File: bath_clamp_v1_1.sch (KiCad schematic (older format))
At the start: 66 parts, among them J1 105-1103-001, J2 105-1103-001, J3 105-1103-001, K1 1462042-8, K2 1462042-8, Q1 MBT3904DW1T1G, Q3 MBT3904DW1T1G, Q4 MBT3904DW1T1G, U1 OPA828, U12 TCA9555DBR, U13 TCA9555DBR, U2 ADG1208, U3 G6L-1F-TR-DC5, U4 G6L-1F-TR-DC5, U5 G6L-1F-TR-DC5

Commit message: made sheet for Howland
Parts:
- removed C?: 5p, Capacitor_SMD:C_0603_1608Metric, symbol Device:C
- removed C? (x2): 0.1u, Capacitor_SMD:C_0603_1608Metric, symbol Device:C
- removed R? (x4): 1M, Resistor_SMD:R_0603_1608Metric, symbol Device:R_US
- removed U?: OPA991S, Package_TO_SOT_SMD:SOT-23-6, symbol covg-kicad:OPA991S
- J4: renamed from J?; footprint (none) -> bath_clamp_v1:HDMI_A
- U19: renamed from U?; footprint PW16_TEX -> Package_SO:TSSOP-16_4.4x5mm_P0.65mm
- gave numbers to parts that had none: 9
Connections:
- wire segments 347 -> 321
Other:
- note removed: "50 nA to 10 uA\n=> 50 mV to 10 V"
- note removed: "Howland Current Pump\nTexas Instrument AN-1515\nR matching sets output impedance\nUse 0.1% tol. Rs"
- note removed: "SDOWN referenced to V-\ninternal pull-down\n"
- moved on the sheet: C29, C30

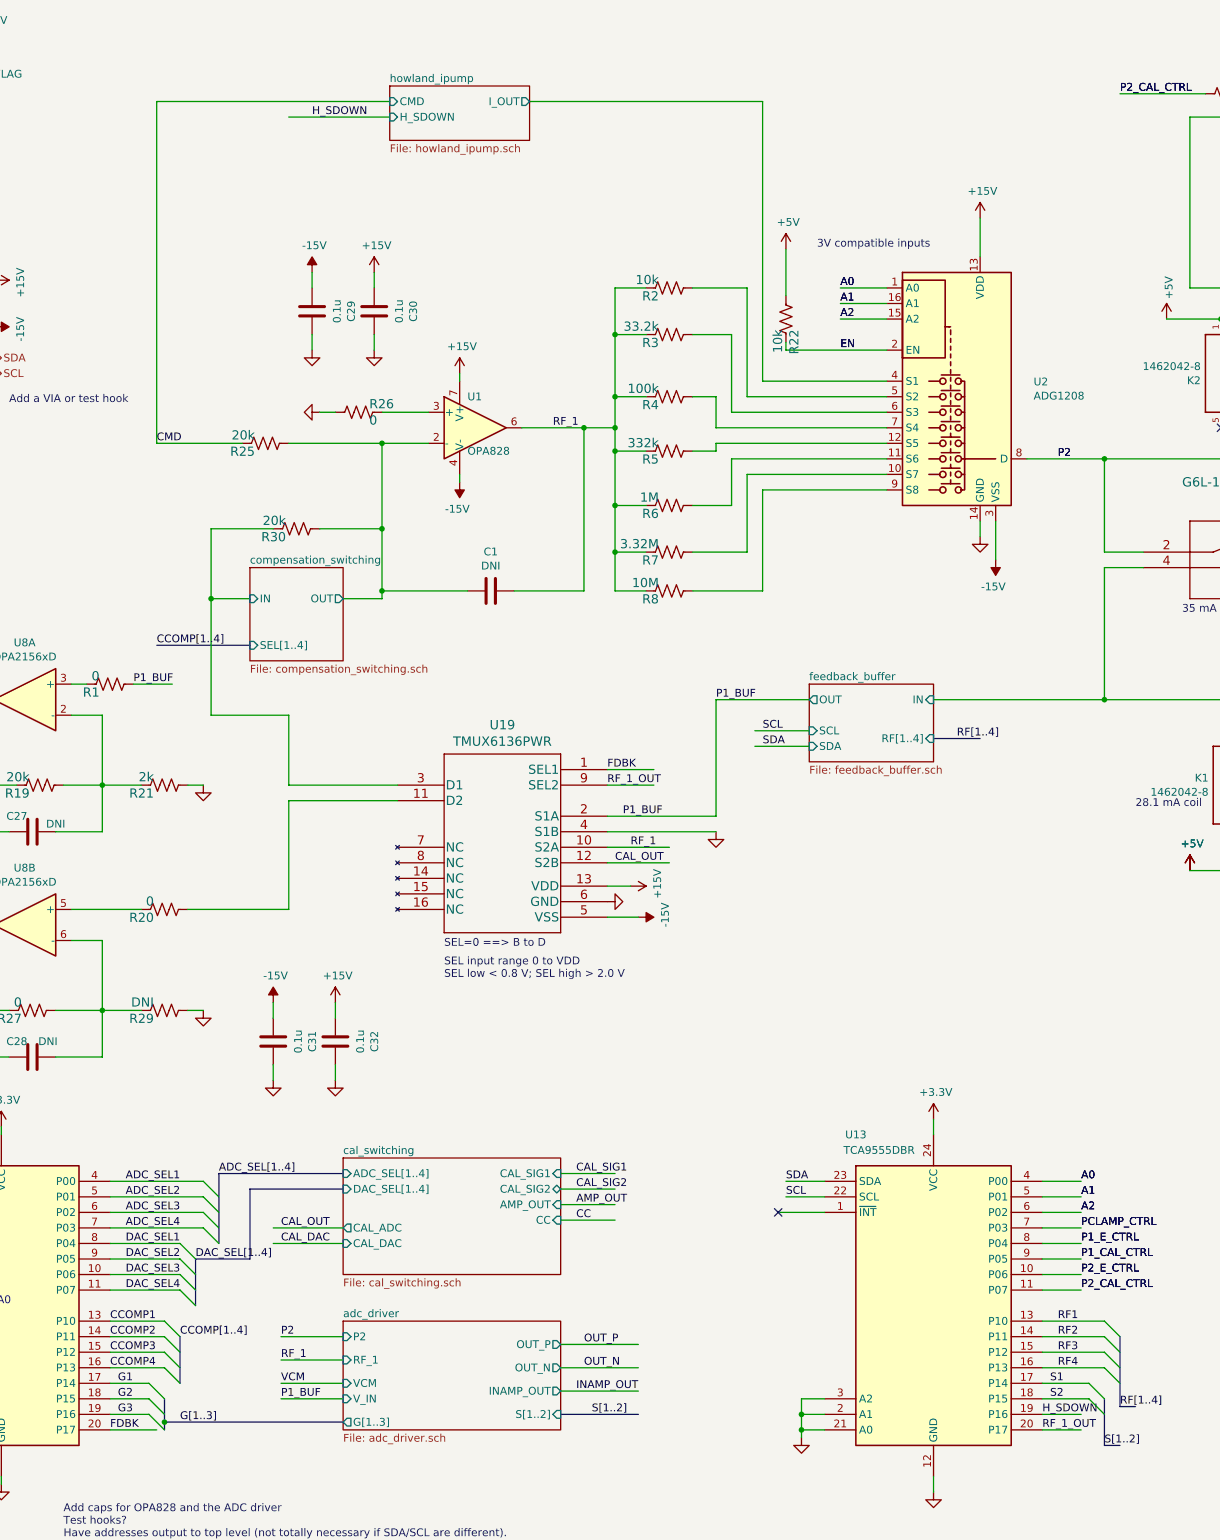
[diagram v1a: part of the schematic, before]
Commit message: removed all references to clamp footprints
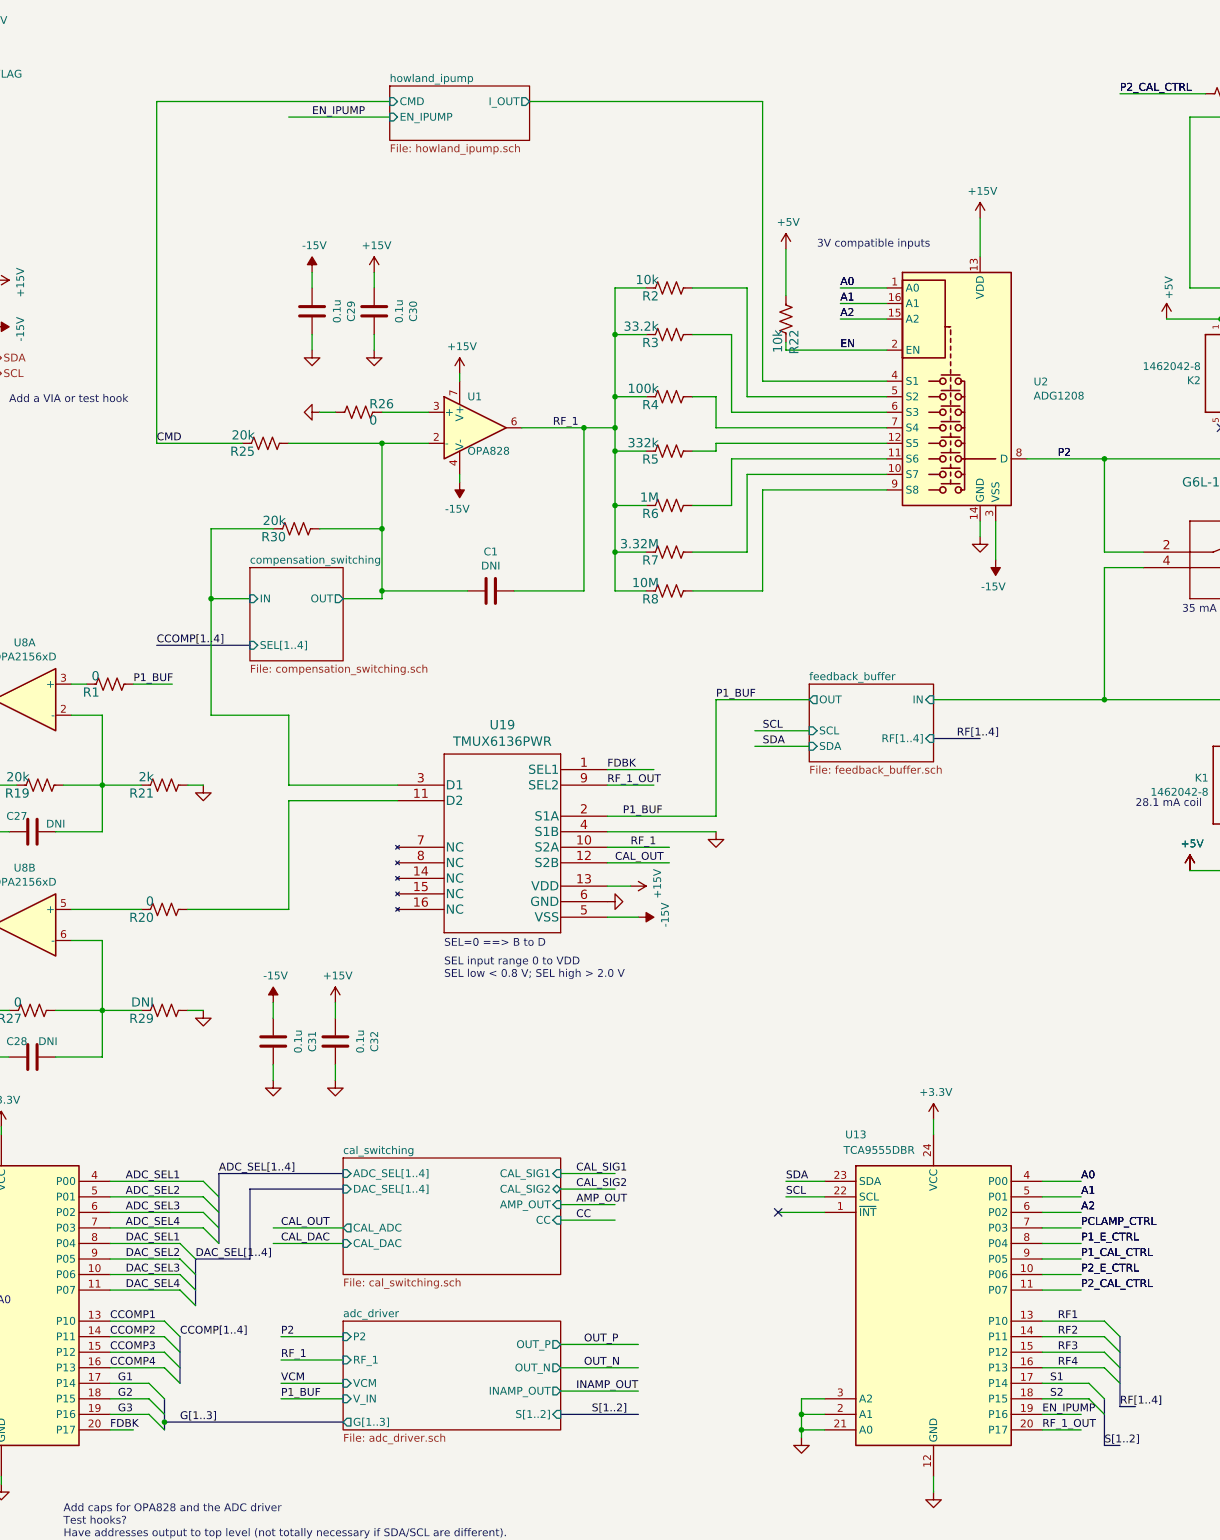
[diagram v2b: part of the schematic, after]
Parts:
- J4: footprint bath_clamp_v1:HDMI_A -> covg-kicad:HDMI_A
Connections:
- net labels added: EN_IPUMP
- net labels removed: H_SDOWN
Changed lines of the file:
@@
 	8800 9550 9050 9550
 Text Label 8800 9550 0    50   ~ 0
-H_SDOWN
+EN_IPUMP
 Wire Wire Line
 	6000 5400 6300 5400
@@
 	3150 9600 3150 9650
 Wire Wire Line
-	2800 9650 3100 9650
-Wire Wire Line
 	6000 5800 6700 5800
 $Comp
@@
 F 0 "J4" H 1680 2496 50  0000 L CNN
 F 1 "HDMI_A" H 1680 2405 50  0000 L CNN
-F 2 "bath_clamp_v1:HDMI_A" H 1275 2450 50  0001 C CNN
+F 2 "covg-kicad:HDMI_A" H 1275 2450 50  0001 C CNN
 F 3 "https://en.wikipedia.org/wiki/HDMI" H 1275 2450 50  0001 C CNN
 	1    1250 2450
@@
 F2 "I_OUT" O R 5500 1100 50
 F3 "CMD" I L 4600 1100 50
-F4 "H_SDOWN" I L 4600 1200 50
+F4 "EN_IPUMP" I L 4600 1200 50
 $EndSheet
 Wire Wire Line
@@
 Wire Wire Line
 	4600 1200 3950 1200
+Text Label 4100 1200 0    50   ~ 0
+EN_IPUMP
+Wire Wire Line
+	2800 9650 2950 9650
 Wire Bus Line
 	9200 9450 9200 9750
@@
 Wire Bus Line
 	3500 8000 3500 8450
-Text Label 4100 1200 0    50   ~ 0
-H_SDOWN
 $EndSCHEMATC

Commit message: layout updates; part positioning
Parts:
- added C36, C38: 0.1u, Capacitor_SMD:C_0603_1608Metric, symbol Device:C
- added C37: DNI, Capacitor_SMD:C_0603_1608Metric, symbol Device:C
- added R63: 30k, Resistor_SMD:R_0603_1608Metric, symbol Device:R_US
- added R64: 3k, Resistor_SMD:R_0603_1608Metric, symbol Device:R_US
- added R67, R69, R70: DNI, Resistor_SMD:R_0603_1608Metric, symbol Device:R_US
- added U25: OPA2156xD, Package_SO:SOIC-8_3.9x4.9mm_P1.27mm, symbol Amplifier_Operational:OPA2156xD
- J4: footprint covg-kicad:HDMI_A -> covg-kicad:CONN_10029449-111RLF_HDMI_A
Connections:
- net labels added: CMD_BUF
- wire segments 321 -> 353
- no-connect marks 5 -> 6
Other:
- note added: "Gain by x10 on cable\nAnd down by x10 on brd\nto reduce cable cross-talk"
- moved on the sheet: C1, C29, C30, J4, R25, R26

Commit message: layout updates and 3d models
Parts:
- added TP? (x8): RCT-0C, digikey-footprints:PROBE_PAD_0805, symbol dk_Test-Points:RCT-0C
- Q1, Q3, Q4: footprint digikey-footprints:SOT-363 -> Package_TO_SOT_SMD:SOT-363_SC-70-6
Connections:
- net labels added: F_MUX_OUT, P1, P1_OUT, P2_OUT, V_GND
- wire segments 353 -> 360
- no-connect marks 6 -> 5
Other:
- note added: "Gain by x10 on cable\nAnd down by x10 on brd\nto reduce impact of \ncable cross-talk"
- note removed: "Add a VIA or test hook"
- note removed: "Gain by x10 on cable\nAnd down by x10 on brd\nto reduce cable cross-talk"

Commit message: updates to README
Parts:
- added C39, C40: 0.1u, Capacitor_SMD:C_0603_1608Metric, symbol Device:C
- J4: Manf# (none) -> 10029449-111RLF
- TP1, TP2, TP3, TP4, TP5, TP6, TP7, TP8: renamed from TP?; Manf# (none) -> RCT-0C
- U12, U13: Manf# (none) -> TCA9555DBR
- U19: Manf# (none) -> TMUX6136PWR
- U25, U8: Manf# (none) -> OPA2156IDR
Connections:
- net labels added: A0_EXP0, A0_EXP1, A1_EXP0, A1_EXP1, A2_EXP0, A2_EXP1
- wire segments 360 -> 358
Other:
- note added: "110"
- note added: "Addr = \n0100_A2_A1_A0"
- note removed: "Add caps for OPA828 and the ADC driver\nTest hooks?\nHave addresses output to top level (not totally necessary if SDA/SCL are different). \n Buffer out calibration switching block."
- note removed: "Addr = 0100_A2_A1_A0"
- moved on the sheet: C31

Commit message: freerouter updates; close to submission
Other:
- moved on the sheet: C30, C37, R69
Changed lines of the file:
@@
 L power:+15V #PWR0154
 U 1 1 61EC7018
-P 5250 1950
+P 5300 1950
 AR Path="/6032F251/61EC7018" Ref="#PWR0154"  Part="1"
 AR Path="/6032F251/608FDC40/61EC7018" Ref="#PWR?"  Part="1"
-F 0 "#PWR0154" H 5250 1800 50  0001 C CNN
-F 1 "+15V" H 5265 2123 50  0000 C CNN
-F 2 "" H 5250 1950 50  0001 C CNN
-F 3 "" H 5250 1950 50  0001 C CNN
-	1    5250 1950
+F 0 "#PWR0154" H 5300 1800 50  0001 C CNN
+F 1 "+15V" H 5315 2123 50  0000 C CNN
+F 2 "" H 5300 1950 50  0001 C CNN
+F 3 "" H 5300 1950 50  0001 C CNN
+	1    5300 1950
 	1    0    0    -1
 $EndComp
@@
 L power:GND #PWR0155
 U 1 1 61EC701E
-P 5250 2450
+P 5300 2450
 AR Path="/6032F251/61EC701E" Ref="#PWR0155"  Part="1"
 AR Path="/6032F251/608FDC40/61EC701E" Ref="#PWR?"  Part="1"
-F 0 "#PWR0155" H 5250 2200 50  0001 C CNN
-F 1 "GND" V 5255 2322 50  0001 R CNN
-F 2 "" H 5250 2450 50  0001 C CNN
-F 3 "" H 5250 2450 50  0001 C CNN
-	1    5250 2450
+F 0 "#PWR0155" H 5300 2200 50  0001 C CNN
+F 1 "GND" V 5305 2322 50  0001 R CNN
+F 2 "" H 5300 2450 50  0001 C CNN
+F 3 "" H 5300 2450 50  0001 C CNN
+	1    5300 2450
 	1    0    0    -1
 $EndComp
@@
 L Device:C C30
 U 1 1 61EC7026
-P 5250 2200
+P 5300 2200
 AR Path="/6032F251/61EC7026" Ref="C30"  Part="1"
 AR Path="/6032F251/608FDC40/61EC7026" Ref="C?"  Part="1"
-F 0 "C30" V 4998 2200 50  0000 C CNN
-F 1 "0.1u" V 5089 2200 50  0000 C CNN
-F 2 "Capacitor_SMD:C_0603_1608Metric" H 5288 2050 50  0001 C CNN
-F 3 "~" H 5250 2200 50  0001 C CNN
-F 4 "CC0603MRX7R8BB104" H 4998 2300 50  0001 C CNN "Manf#"
-F 5 "25V" H 4998 2300 50  0001 C CNN "voltage"
-	1    5250 2200
+F 0 "C30" V 5048 2200 50  0000 C CNN
+F 1 "0.1u" V 5139 2200 50  0000 C CNN
+F 2 "Capacitor_SMD:C_0603_1608Metric" H 5338 2050 50  0001 C CNN
+F 3 "~" H 5300 2200 50  0001 C CNN
+F 4 "CC0603MRX7R8BB104" H 5048 2300 50  0001 C CNN "Manf#"
+F 5 "25V" H 5048 2300 50  0001 C CNN "voltage"
+	1    5300 2200
 	-1   0    0    1
 $EndComp
@@
 	4850 2050 4850 1950
 Wire Wire Line
-	5250 2450 5250 2350
-Wire Wire Line
-	5250 2050 5250 1950
+	5300 2450 5300 2350
+Wire Wire Line
+	5300 2050 5300 1950
 Wire Wire Line
 	6000 5800 6700 5800
@@
 L Device:R_US R69
 U 1 1 60DC88BE
-P 4250 2900
-F 0 "R69" V 4197 2968 59  0000 L CNN
-F 1 "DNI" V 4302 2968 59  0000 L CNN
-F 2 "Resistor_SMD:R_0603_1608Metric" H 4250 2900 50  0001 C CNN
-F 3 "" H 4250 2900 50  0001 C CNN
-F 4 "" H 4197 3068 50  0001 C CNN "Manf#"
-F 5 "1%" H 4250 2900 50  0001 C CNN "Tolerance"
-	1    4250 2900
+P 4250 2750
+F 0 "R69" V 4197 2818 59  0000 L CNN
+F 1 "DNI" V 4302 2818 59  0000 L CNN
+F 2 "Resistor_SMD:R_0603_1608Metric" H 4250 2750 50  0001 C CNN
+F 3 "" H 4250 2750 50  0001 C CNN
+F 4 "" H 4197 2918 50  0001 C CNN "Manf#"
+F 5 "1%" H 4250 2750 50  0001 C CNN "Tolerance"
+	1    4250 2750
 	-1   0    0    1
 $EndComp
@@
 L Device:C C37
 U 1 1 60DC916C
-P 4250 2400
+P 4250 2350
 AR Path="/6032F251/60DC916C" Ref="C37"  Part="1"
 AR Path="/6032F251/608FDC40/60DC916C" Ref="C?"  Part="1"
-F 0 "C37" V 3998 2400 50  0000 C CNN
-F 1 "DNI" V 4089 2400 50  0000 C CNN
-F 2 "Capacitor_SMD:C_0603_1608Metric" H 4288 2250 50  0001 C CNN
-F 3 "~" H 4250 2400 50  0001 C CNN
-F 4 "CC0603MRX7R8BB104" H 3998 2500 50  0001 C CNN "Manf#"
-F 5 "20%" H 3998 2500 50  0001 C CNN "Tolerance"
-F 6 "25V" H 3998 2500 50  0001 C CNN "voltage"
-	1    4250 2400
+F 0 "C37" V 3998 2350 50  0000 C CNN
+F 1 "DNI" V 4089 2350 50  0000 C CNN
+F 2 "Capacitor_SMD:C_0603_1608Metric" H 4288 2200 50  0001 C CNN
+F 3 "~" H 4250 2350 50  0001 C CNN
+F 4 "CC0603MRX7R8BB104" H 3998 2450 50  0001 C CNN "Manf#"
+F 5 "20%" H 3998 2450 50  0001 C CNN "Tolerance"
+F 6 "25V" H 3998 2450 50  0001 C CNN "voltage"
+	1    4250 2350
 	-1   0    0    1
 $EndComp
@@
 $EndComp
 Wire Wire Line
-	4250 2050 4250 2250
+	4250 2050 4250 2200
 $Comp
 L Amplifier_Operational:OPA2156xD U25
@@
 	4050 3300 4250 3300
 Wire Wire Line
-	4250 2750 4250 2550
-Wire Wire Line
-	4250 3050 4250 3300
+	4250 2600 4250 2500
+Wire Wire Line
+	4250 2900 4250 3300
 Connection ~ 4250 3300
 Wire Wire Line

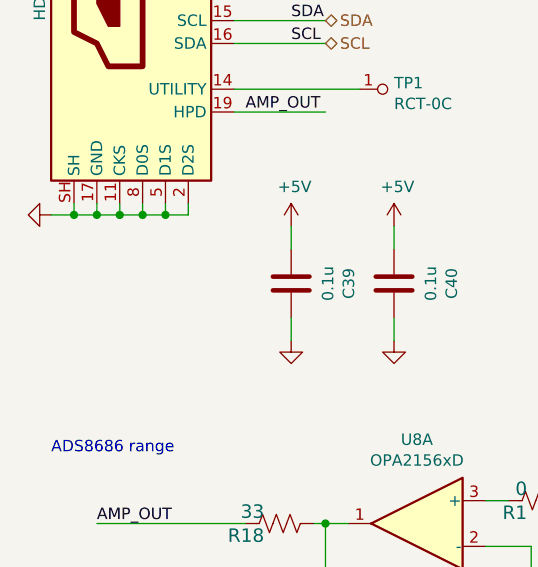
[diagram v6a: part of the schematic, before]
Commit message: updates to schematic plot
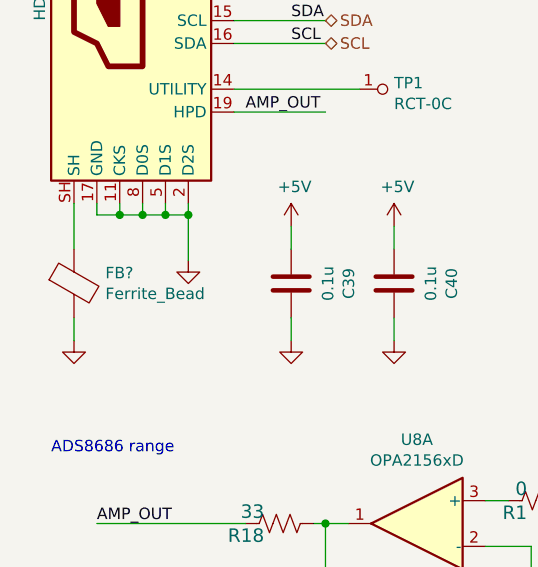
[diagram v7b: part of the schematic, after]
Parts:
- added FB?: Ferrite_Bead, Capacitor_SMD:C_1206_3216Metric, symbol Device:Ferrite_Bead
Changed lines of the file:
@@
 L power:GND #PWR0127
 U 1 1 60605E23
-P 650 3600
-F 0 "#PWR0127" H 650 3350 50  0001 C CNN
-F 1 "GND" V 655 3472 50  0001 R CNN
-F 2 "" H 650 3600 50  0001 C CNN
-F 3 "" H 650 3600 50  0001 C CNN
-	1    650  3600
-	0    1    1    0
+P 1250 3800
+F 0 "#PWR0127" H 1250 3550 50  0001 C CNN
+F 1 "GND" V 1255 3672 50  0001 R CNN
+F 2 "" H 1250 3800 50  0001 C CNN
+F 3 "" H 1250 3800 50  0001 C CNN
+	1    1250 3800
+	1    0    0    -1
 $EndComp
 Wire Wire Line
@@
 Connection ~ 1050 3600
 Wire Wire Line
-	750  3600 750  3550
-Connection ~ 750  3600
-Wire Wire Line
-	850  3600 750  3600
-Wire Wire Line
-	750  3600 650  3600
-Wire Wire Line
 	850  3550 850  3600
-Connection ~ 850  3600
 Wire Wire Line
 	950  3600 850  3600
@@
 	1    0    0    -1
 $EndComp
+Wire Wire Line
+	1250 3800 1250 3600
+Connection ~ 1250 3600
+$Comp
+L Device:Ferrite_Bead FB?
+U 1 1 61B9C943
+P 750 3900
+F 0 "FB?" H 887 3946 50  0000 L CNN
+F 1 "Ferrite_Bead" H 887 3855 50  0000 L CNN
+F 2 "Capacitor_SMD:C_1206_3216Metric" V 680 3900 50  0001 C CNN
+F 3 "~" H 750 3900 50  0001 C CNN
+F 4 "BLM31PG500SN1L" H 750 3900 50  0001 C CNN "Manf#"
+	1    750  3900
+	1    0    0    -1
+$EndComp
+$Comp
+L power:GND #PWR?
+U 1 1 61B9CF45
+P 750 4150
+AR Path="/6032F251/61B9CF45" Ref="#PWR?"  Part="1"
+AR Path="/6032F251/608FDC40/61B9CF45" Ref="#PWR?"  Part="1"
+F 0 "#PWR?" H 750 3900 50  0001 C CNN
+F 1 "GND" V 755 4022 50  0001 R CNN
+F 2 "" H 750 4150 50  0001 C CNN
+F 3 "" H 750 4150 50  0001 C CNN
+	1    750  4150
+	1    0    0    -1
+$EndComp
+Wire Wire Line
+	750  4150 750  4050
+Wire Wire Line
+	750  3550 750  3750
 Wire Bus Line
 	9200 9450 9200 9750
